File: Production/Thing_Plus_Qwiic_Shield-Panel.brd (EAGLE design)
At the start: 22.9 x 50.8 mm, 32 parts, among them J1 QWIIC_RIGHT_ANGLE, J2 QWIIC_RIGHT_ANGLE, J3 Vertical Qwiic Connector, J4 Vertical Qwiic Connector, J5 THING_PLUS

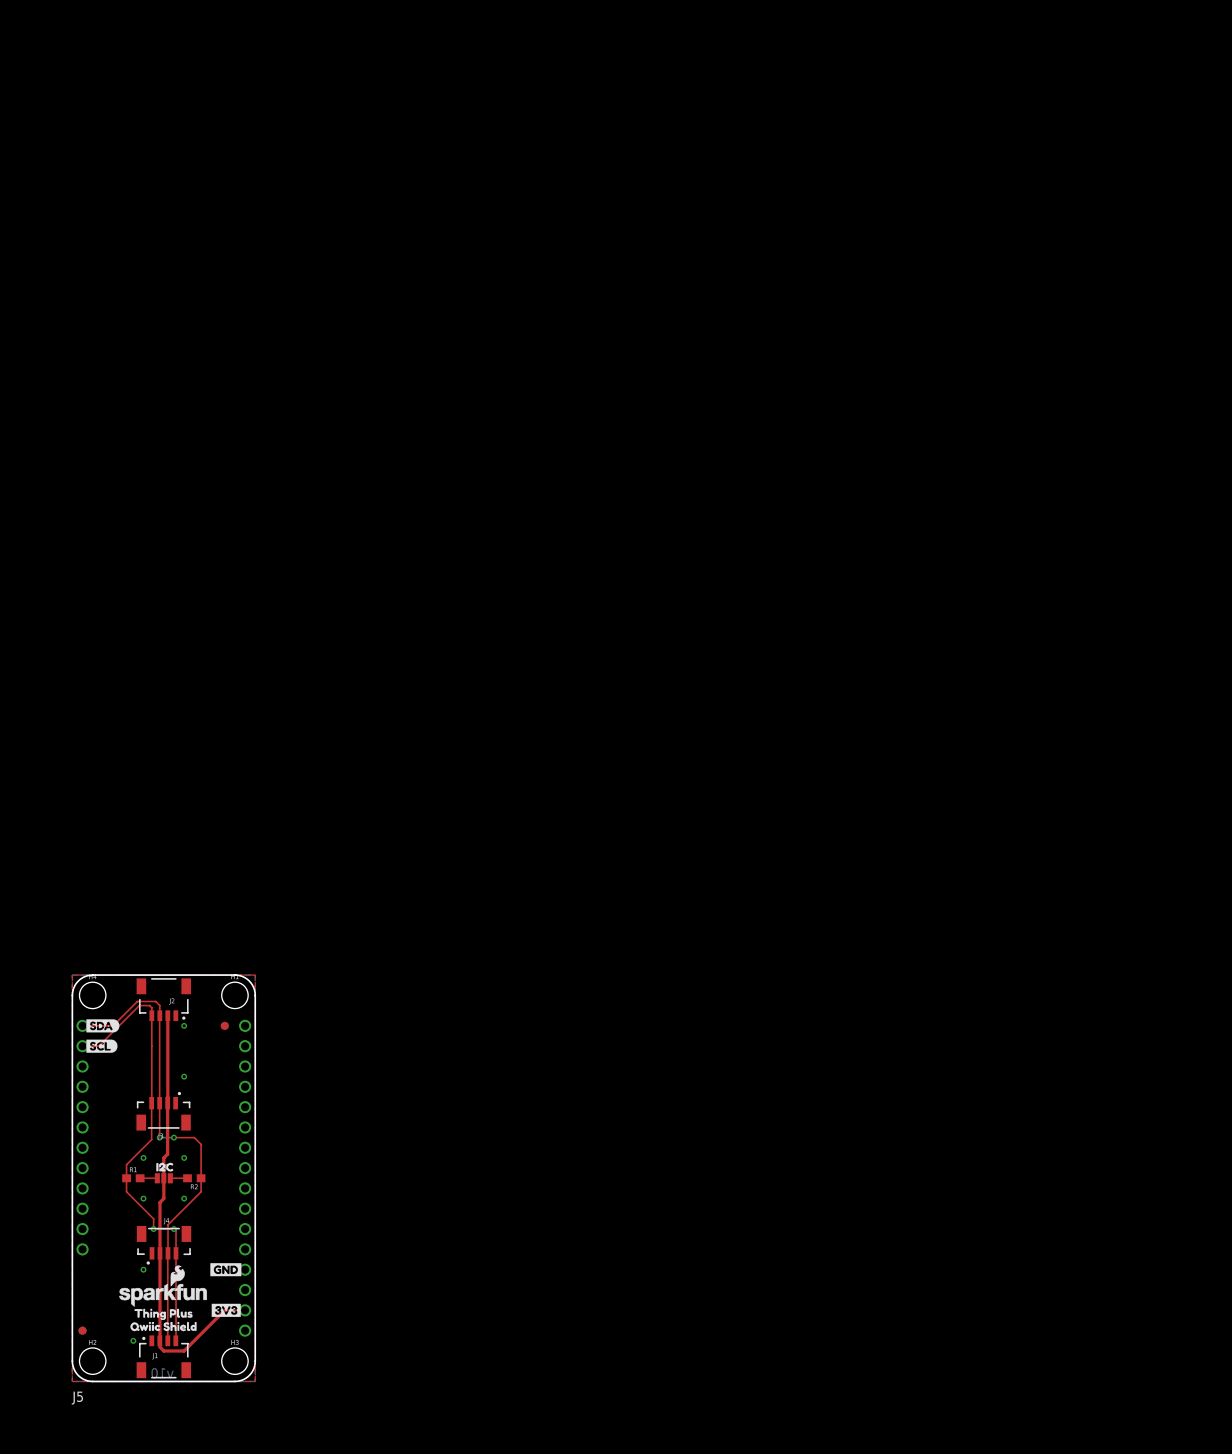
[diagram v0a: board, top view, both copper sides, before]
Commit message: panelizing and uploading gerbers
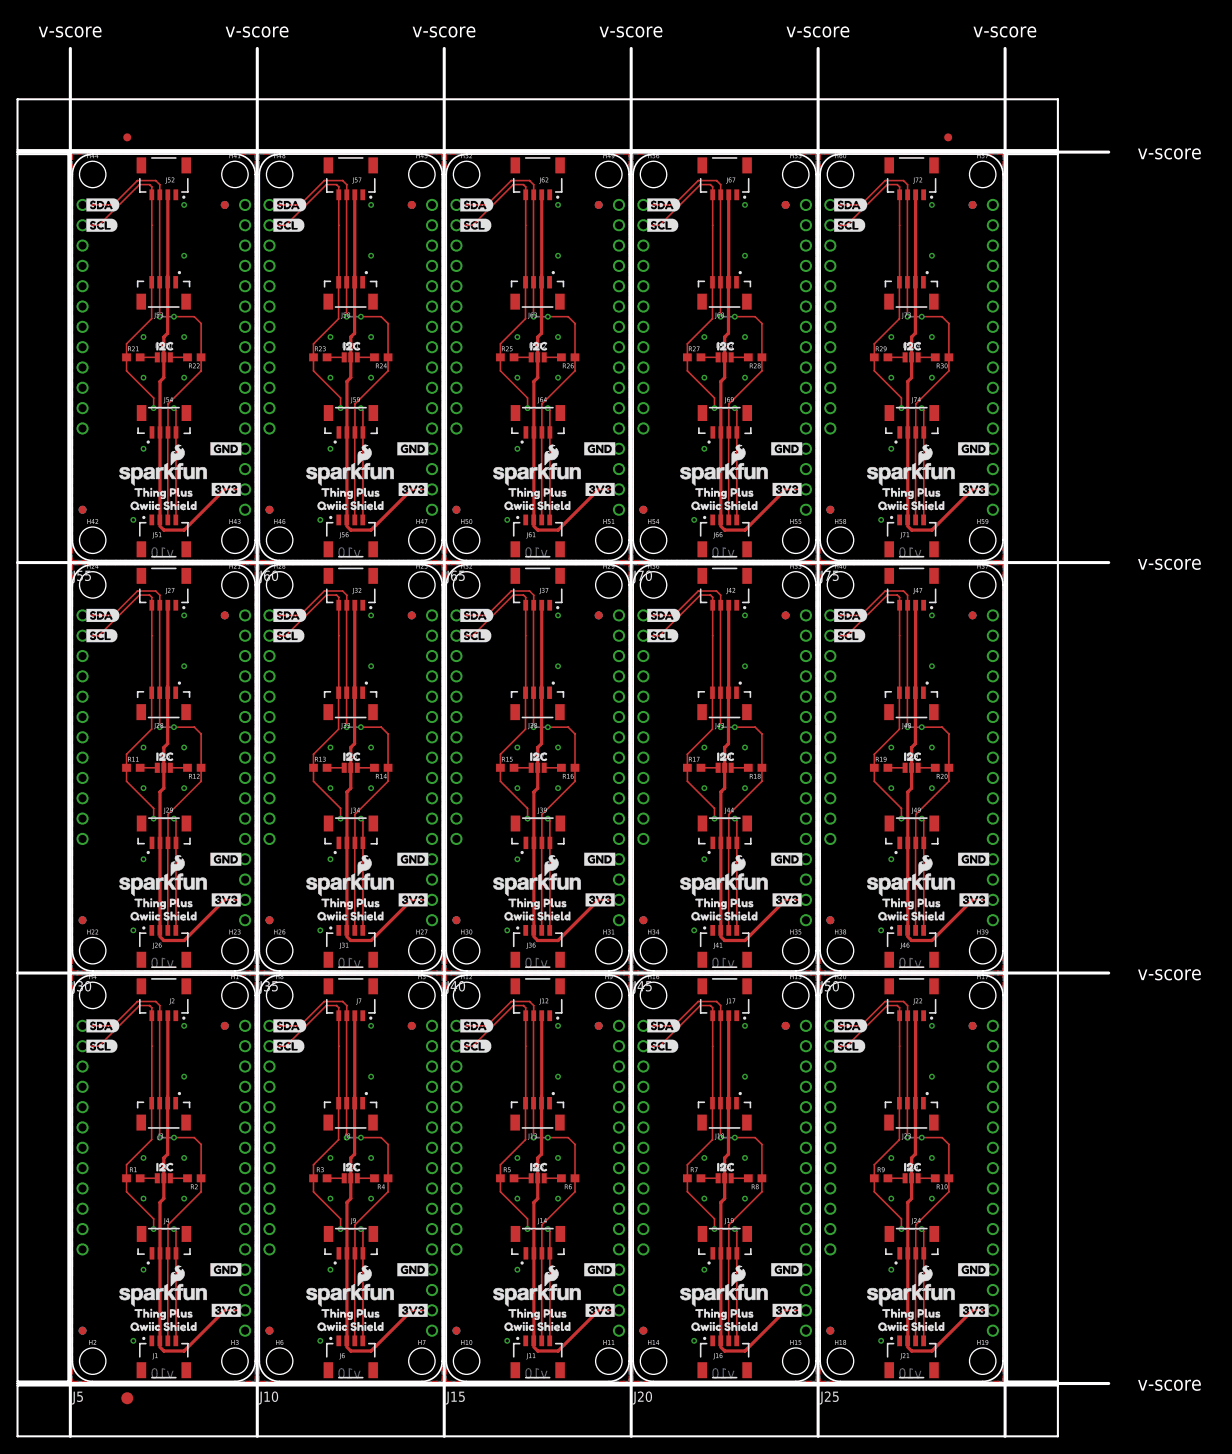
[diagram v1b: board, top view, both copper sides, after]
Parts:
- removed FRAME1: FRAME-LETTER, SparkFun-Aesthetics:CREATIVE_COMMONS
- added E$1, E$2: (no value), SparkFun-Aesthetics:FIDUCIAL-1X2
- added E$3: (no value), SparkFun-Retired:FIDUCIAL-1.5X3
- added FD10, FD11, FD12, FD13, FD14, FD15, FD16, FD17, FD18, FD19, FD20, FD21, FD22, FD23, FD24, FD25, FD26, FD27, FD28, FD29, FD30, FD31, FD32, FD33, FD34, FD35, FD36, FD37, FD38, FD39, FD40, FD41, FD42, FD43, FD44, FD45, FD46, FD47, FD48, FD49, FD5, FD50, FD51, FD52, FD53, FD54, FD55, FD56, FD57, FD58, FD59, FD6, FD60, FD7, FD8, FD9: FIDUCIAL1X2, SparkFun-Aesthetics:FIDUCIAL-1X2
- added H10, H11, H12, H13, H14, H15, H16, H17, H18, H19, H20, H21, H22, H23, H24, H25, H26, H27, H28, H29, H30, H31, H32, H33, H34, H35, H36, H37, H38, H39, H40, H41, H42, H43, H44, H45, H46, H47, H48, H49, H5, H50, H51, H52, H53, H54, H55, H56, H57, H58, H59, H6, H60, H7, H8, H9: STAND-OFF, SparkFun-Hardware:STAND-OFF
- added I2C1, I2C10, I2C11, I2C12, I2C13, I2C14, I2C2, I2C3, I2C4, I2C5, I2C6, I2C7, I2C8, I2C9: JUMPER-SMT_3_NO_NO-SILK, SparkFun-Jumpers:SMT-JUMPER_3_NO_NO-SILK
- added J10, J15, J20, J25, J30, J35, J40, J45, J50, J55, J60, J65, J70, J75: THING_PLUS, SparkFun-Boards:THING_PLUS
- added J11, J12, J16, J17, J21, J22, J26, J27, J31, J32, J36, J37, J41, J42, J46, J47, J51, J52, J56, J57, J6, J61, J62, J66, J67, J7, J71, J72: QWIIC_RIGHT_ANGLE, SparkFun-Connectors:JST04_1MM_RA
- added J13, J14, J18, J19, J23, J24, J28, J29, J33, J34, J38, J39, J43, J44, J48, J49, J53, J54, J58, J59, J63, J64, J68, J69, J73, J74, J8, J9: Vertical Qwiic Connector, SparkFun-Connectors:JST04_1MM_VERT
- added LOGO10, LOGO13, LOGO16, LOGO19, LOGO22, LOGO25, LOGO28, LOGO31, LOGO34, LOGO37, LOGO4, LOGO40, LOGO43, LOGO7: SFE_LOGO_NAME_FLAME.1_INCH, SparkFun-Aesthetics:SFE_LOGO_NAME_FLAME_.1
- added LOGO11, LOGO14, LOGO17, LOGO20, LOGO23, LOGO26, LOGO29, LOGO32, LOGO35, LOGO38, LOGO41, LOGO44, LOGO5, LOGO8: SFE_LOGO_NAME_FLAME.2_INCH, SparkFun-Aesthetics:SFE_LOGO_NAME_FLAME_.2
- added LOGO12, LOGO15, LOGO18, LOGO21, LOGO24, LOGO27, LOGO30, LOGO33, LOGO36, LOGO39, LOGO42, LOGO45, LOGO6, LOGO9: OSHW-LOGOS, SparkFun-Aesthetics:OSHW-LOGO-S
- added R10, R11, R12, R13, R14, R15, R16, R17, R18, R19, R20, R21, R22, R23, R24, R25, R26, R27, R28, R29, R3, R30, R4, R5, R6, R7, R8, R9: 4.7k, SparkFun-Resistors:0603
- added U$100, U$101, U$112, U$113, U$124, U$125, U$136, U$137, U$148, U$149, U$16, U$160, U$161, U$17, U$172, U$173, U$28, U$29, U$40, U$41, U$52, U$53, U$64, U$65, U$76, U$77, U$88, U$89: (no value), buzzard_labels (23):3V36
- added U$102, U$103, U$114, U$115, U$126, U$127, U$138, U$139, U$150, U$151, U$162, U$163, U$174, U$175, U$18, U$19, U$30, U$31, U$42, U$43, U$54, U$55, U$66, U$67, U$78, U$79, U$90, U$91: (no value), buzzard_labels (23):GND0
- added U$104, U$116, U$128, U$140, U$152, U$164, U$176, U$20, U$32, U$44, U$56, U$68, U$80, U$92: (no value), buzzard_labels (23):I2C5
- added U$105, U$117, U$129, U$141, U$153, U$165, U$177, U$21, U$33, U$45, U$57, U$69, U$81, U$93: (no value), buzzard_labels (26):SCL1
- added U$106, U$118, U$130, U$142, U$154, U$166, U$178, U$22, U$34, U$46, U$58, U$70, U$82, U$94: (no value), buzzard_labels (26):SCL3
- added U$107, U$119, U$131, U$143, U$155, U$167, U$179, U$23, U$35, U$47, U$59, U$71, U$83, U$95: (no value), buzzard_labels (26):SDA0
- added U$108, U$120, U$132, U$144, U$156, U$168, U$180, U$24, U$36, U$48, U$60, U$72, U$84, U$96: (no value), buzzard_labels (26):SDA2
- added U$109, U$121, U$13, U$133, U$145, U$157, U$169, U$25, U$37, U$49, U$61, U$73, U$85, U$97: (no value), buzzard_labels (25):THING_PLUS0
- added U$110, U$122, U$134, U$14, U$146, U$158, U$170, U$26, U$38, U$50, U$62, U$74, U$86, U$98: (no value), buzzard_labels (25):_QWIIC_SHIELD1
- added U$111, U$123, U$135, U$147, U$15, U$159, U$171, U$27, U$39, U$51, U$63, U$75, U$87, U$99: (no value), buzzard_labels (24):3V36
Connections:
- new net 3.3V1: I2C1.2, J10.27, J6.2, J7.2, J8.2, J9.2
- new net 3.3V10: I2C10.2, J51.2, J52.2, J53.2, J54.2, J55.27
- new net 3.3V11: I2C11.2, J56.2, J57.2, J58.2, J59.2, J60.27
- new net 3.3V12: I2C12.2, J61.2, J62.2, J63.2, J64.2, J65.27
- new net 3.3V13: I2C13.2, J66.2, J67.2, J68.2, J69.2, J70.27
- new net 3.3V14: I2C14.2, J71.2, J72.2, J73.2, J74.2, J75.27
- new net 3.3V2: I2C2.2, J11.2, J12.2, J13.2, J14.2, J15.27
- new net 3.3V3: I2C3.2, J16.2, J17.2, J18.2, J19.2, J20.27
- new net 3.3V4: I2C4.2, J21.2, J22.2, J23.2, J24.2, J25.27
- new net 3.3V5: I2C5.2, J26.2, J27.2, J28.2, J29.2, J30.27
- new net 3.3V6: I2C6.2, J31.2, J32.2, J33.2, J34.2, J35.27
- new net 3.3V7: I2C7.2, J36.2, J37.2, J38.2, J39.2, J40.27
- new net 3.3V8: I2C8.2, J41.2, J42.2, J43.2, J44.2, J45.27
- new net 3.3V9: I2C9.2, J46.2, J47.2, J48.2, J49.2, J50.27
- new net GND1: J10.25, J6.1, J7.1, J8.1, J9.1
- new net GND10: J51.1, J52.1, J53.1, J54.1, J55.25
- new net GND11: J56.1, J57.1, J58.1, J59.1, J60.25
- new net GND12: J61.1, J62.1, J63.1, J64.1, J65.25
- new net GND13: J66.1, J67.1, J68.1, J69.1, J70.25
- new net GND14: J71.1, J72.1, J73.1, J74.1, J75.25
- new net GND2: J11.1, J12.1, J13.1, J14.1, J15.25
- new net GND3: J16.1, J17.1, J18.1, J19.1, J20.25
- new net GND4: J21.1, J22.1, J23.1, J24.1, J25.25
- new net GND5: J26.1, J27.1, J28.1, J29.1, J30.25
- new net GND6: J31.1, J32.1, J33.1, J34.1, J35.25
- new net GND7: J36.1, J37.1, J38.1, J39.1, J40.25
- new net GND8: J41.1, J42.1, J43.1, J44.1, J45.25
- new net GND9: J46.1, J47.1, J48.1, J49.1, J50.25
- new net N$1: I2C1.3, R4.2
- new net N$10: I2C4.1, R9.2
- new net N$11: I2C5.3, R12.2
- new net N$12: I2C5.1, R11.2
- new net N$13: I2C6.3, R14.2
- new net N$14: I2C6.1, R13.2
- new net N$15: I2C7.3, R16.2
- new net N$16: I2C7.1, R15.2
- new net N$17: I2C8.3, R18.2
- new net N$18: I2C8.1, R17.2
- new net N$19: I2C9.3, R20.2
- new net N$2: I2C1.1, R3.2
- new net N$20: I2C9.1, R19.2
- new net N$21: I2C10.3, R22.2
- new net N$22: I2C10.1, R21.2
- new net N$23: I2C11.3, R24.2
- new net N$24: I2C11.1, R23.2
- new net N$25: I2C12.3, R26.2
- new net N$26: I2C12.1, R25.2
- new net N$27: I2C13.3, R28.2
- new net N$28: I2C13.1, R27.2
- new net N$29: I2C14.3, R30.2
- new net N$30: I2C14.1, R29.2
- new net N$5: I2C2.3, R6.2
- new net N$6: I2C2.1, R5.2
- new net N$7: I2C3.3, R8.2
- new net N$8: I2C3.1, R7.2
- new net N$9: I2C4.3, R10.2
- new net SCL1: J10.2, J6.4, J7.4, J8.4, J9.4, R3.1
- new net SCL10: J51.4, J52.4, J53.4, J54.4, J55.2, R21.1
- new net SCL11: J56.4, J57.4, J58.4, J59.4, J60.2, R23.1
- new net SCL12: J61.4, J62.4, J63.4, J64.4, J65.2, R25.1
- new net SCL13: J66.4, J67.4, J68.4, J69.4, J70.2, R27.1
- new net SCL14: J71.4, J72.4, J73.4, J74.4, J75.2, R29.1
- new net SCL2: J11.4, J12.4, J13.4, J14.4, J15.2, R5.1
- new net SCL3: J16.4, J17.4, J18.4, J19.4, J20.2, R7.1
- new net SCL4: J21.4, J22.4, J23.4, J24.4, J25.2, R9.1
- new net SCL5: J26.4, J27.4, J28.4, J29.4, J30.2, R11.1
- new net SCL6: J31.4, J32.4, J33.4, J34.4, J35.2, R13.1
- new net SCL7: J36.4, J37.4, J38.4, J39.4, J40.2, R15.1
- new net SCL8: J41.4, J42.4, J43.4, J44.4, J45.2, R17.1
- new net SCL9: J46.4, J47.4, J48.4, J49.4, J50.2, R19.1
- new net SDA1: J10.1, J6.3, J7.3, J8.3, J9.3, R4.1
- new net SDA10: J51.3, J52.3, J53.3, J54.3, J55.1, R22.1
- new net SDA11: J56.3, J57.3, J58.3, J59.3, J60.1, R24.1
- new net SDA12: J61.3, J62.3, J63.3, J64.3, J65.1, R26.1
- new net SDA13: J66.3, J67.3, J68.3, J69.3, J70.1, R28.1
- new net SDA14: J71.3, J72.3, J73.3, J74.3, J75.1, R30.1
- new net SDA2: J11.3, J12.3, J13.3, J14.3, J15.1, R6.1
- new net SDA3: J16.3, J17.3, J18.3, J19.3, J20.1, R8.1
- new net SDA4: J21.3, J22.3, J23.3, J24.3, J25.1, R10.1
- new net SDA5: J26.3, J27.3, J28.3, J29.3, J30.1, R12.1
- new net SDA6: J31.3, J32.3, J33.3, J34.3, J35.1, R14.1
- new net SDA7: J36.3, J37.3, J38.3, J39.3, J40.1, R16.1
- new net SDA8: J41.3, J42.3, J43.3, J44.3, J45.1, R18.1
- new net SDA9: J46.3, J47.3, J48.3, J49.3, J50.1, R20.1
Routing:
- net SDA3: track 0.00 -> 59.4 mm, vias 0 -> 2
- net SDA13: track 0.00 -> 59.4 mm, vias 0 -> 2
- net SDA8: track 0.00 -> 59.4 mm, vias 0 -> 2
- net SDA9: track 0.00 -> 59.4 mm, vias 0 -> 2
- net SDA7: track 0.00 -> 59.4 mm, vias 0 -> 2
- net SDA12: track 0.00 -> 59.4 mm, vias 0 -> 2
- net SDA14: track 0.00 -> 59.4 mm, vias 0 -> 2
- net SDA10: track 0.00 -> 59.4 mm, vias 0 -> 2
- net SDA6: track 0.00 -> 59.4 mm, vias 0 -> 2
- net SDA5: track 0.00 -> 59.4 mm, vias 0 -> 2
- net SDA4: track 0.00 -> 59.4 mm, vias 0 -> 2
- net SDA2: track 0.00 -> 59.4 mm, vias 0 -> 2
- net SDA11: track 0.00 -> 59.4 mm, vias 0 -> 2
- net SDA1: track 0.00 -> 59.4 mm, vias 0 -> 2
- net SCL3: track 0.00 -> 57.9 mm, vias 0 -> 2
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- added copper zone on layer 1, net GND1
- added copper zone on layer 16, net GND1
- added copper zone on layer 1, net GND10
- added copper zone on layer 16, net GND10
- added copper zone on layer 1, net GND11
- added copper zone on layer 16, net GND11
- added copper zone on layer 1, net GND12
- added copper zone on layer 16, net GND12
- added copper zone on layer 1, net GND13
- added copper zone on layer 16, net GND13
- added copper zone on layer 1, net GND14
- added copper zone on layer 16, net GND14
- added copper zone on layer 1, net GND2
- added copper zone on layer 16, net GND2
- added copper zone on layer 1, net GND3
- added copper zone on layer 16, net GND3
- added copper zone on layer 1, net GND4
- added copper zone on layer 16, net GND4
- added copper zone on layer 1, net GND5
- added copper zone on layer 16, net GND5
- added copper zone on layer 1, net GND6
- added copper zone on layer 16, net GND6
- added copper zone on layer 1, net GND7
- added copper zone on layer 16, net GND7
- added copper zone on layer 1, net GND8
- added copper zone on layer 16, net GND8
- added copper zone on layer 1, net GND9
- added copper zone on layer 16, net GND9
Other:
- board size 22.9 x 50.8 mm -> 136.4 x 173.5 mm
- board text added: "v-score"
- board text removed: "A. England"
